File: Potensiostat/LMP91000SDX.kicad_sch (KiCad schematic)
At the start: 5 parts, among them J1 Conn_01x03_Pin, U2 LMP91000SDX/NOPB

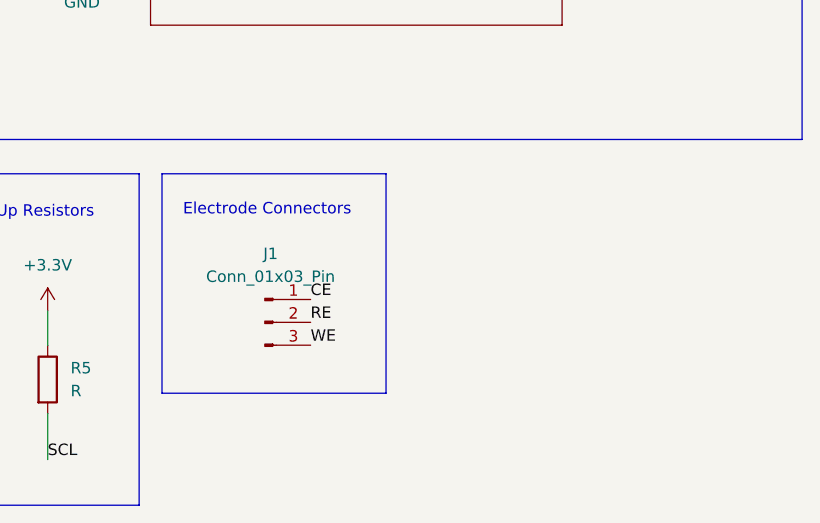
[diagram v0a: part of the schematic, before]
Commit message: Added LMP USP-UART
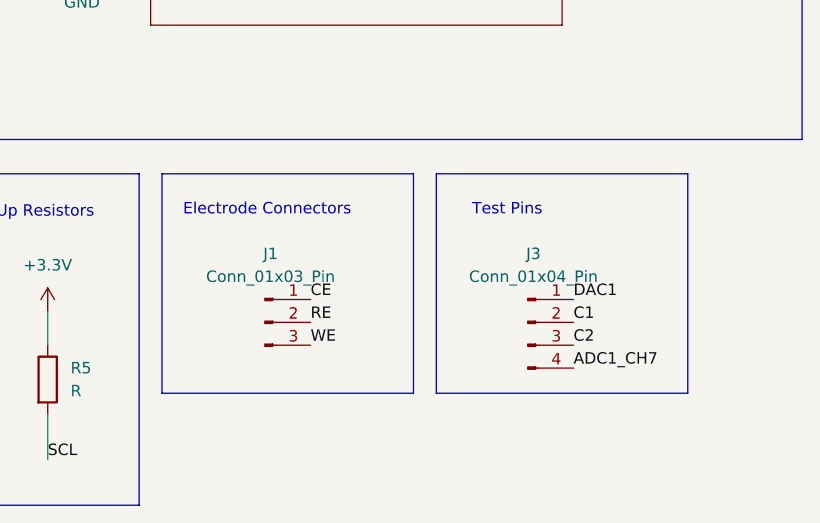
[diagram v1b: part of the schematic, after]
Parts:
- added J3: Conn_01x04_Pin, symbol Connector:Conn_01x04_Pin
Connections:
- net ADC1_CH7: now also J3.4 (Pin_4)
- net C1: now also J3.2 (Pin_2)
- net C2: now also J3.3 (Pin_3)
- net DAC1: now also J3.1 (Pin_1)
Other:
- note added: "Test Pins"
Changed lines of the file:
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@@
 	(rectangle
 		(start 53.34 107.95)
-		(end 78.232 132.334)
+		(end 81.28 132.334)
+		(stroke
+			(width 0)
+			(type default)
+		)
+		(fill
+			(type none)
+		)
+	)
+	(rectangle
+		(start 83.82 107.95)
+		(end 111.76 132.334)
 		(stroke
 			(width 0)
@@
 		(exclude_from_sim no)
 		(at 25.654 21.082 0)
+		(effects
+			(font
+				(size 1.27 1.27)
+			)
+		)
+	)
+	(text "Test Pins"
+		(exclude_from_sim no)
+		(at 91.694 112.014 0)
 		(effects
 			(font
@@
 		)
 	)
+	(label "C2"
+		(at 99.06 127 0)
+		(effects
+			(font
+				(size 1.27 1.27)
+			)
+			(justify left bottom)
+		)
+	)
 	(label "SDA"
 		(at 44.45 76.2 180)
@@
 		)
 	)
+	(label "C1"
+		(at 99.06 124.46 0)
+		(effects
+			(font
+				(size 1.27 1.27)
+			)
+			(justify left bottom)
+		)
+	)
 	(label "SCL"
 		(at 44.45 73.66 180)
@@
 		)
 	)
+	(label "DAC1"
+		(at 99.06 121.92 0)
+		(effects
+			(font
+				(size 1.27 1.27)
+			)
+			(justify left bottom)
+		)
+	)
 	(label "C1"
 		(at 105.41 81.28 0)
@@
 	(label "WE"
 		(at 105.41 76.2 0)
+		(effects
+			(font
+				(size 1.27 1.27)
+			)
+			(justify left bottom)
+		)
+	)
+	(label "ADC1_CH7"
+		(at 99.06 129.54 0)
 		(effects
 			(font
@@
 					(unit 1)
 				)
+			)
+		)
+	)
+	(symbol
+		(lib_id "Connector:Conn_01x04_Pin")
+		(at 93.98 124.46 0)
+		(unit 1)
+		(exclude_from_sim no)
+		(in_bom yes)
+		(on_board yes)
+		(dnp no)
+		(fields_autoplaced yes)
+		(property "Reference" "J3"
+			(at 94.615 116.84 0)
+			(effects
+				(font
+					(size 1.27 1.27)
+				)
+			)
+		)
+		(property "Value" "Conn_01x04_Pin"
+			(at 94.615 119.38 0)
+			(effects
+				(font
+					(size 1.27 1.27)
+				)
+			)
+		)
+		(property "Footprint" ""
+			(at 93.98 124.46 0)
+			(effects
+				(font
+					(size 1.27 1.27)
+				)
+				(hide yes)
+			)
+		)
+		(property "Datasheet" "~"
+			(at 93.98 124.46 0)
+			(effects
+				(font
+					(size 1.27 1.27)
+				)
+				(hide yes)
+			)
+		)
+		(property "Description" "Generic connector, single row, 01x04, script generated"
+			(at 93.98 124.46 0)
+			(effects
+				(font
+					(size 1.27 1.27)
+				)
+				(hide yes)
+			)
+		)
+		(pin "4"
+		)
+		(pin "1"
+		)
+		(pin "2"
+		)
+		(pin "3"
+		)
+		(instances
+			(project ""
+				(path "/be108998-ac86-4f7d-931a-841db1905f2a/62dba8b7-8e77-43af-b2ef-391554dc76c9"
+					(reference "J3")
+					(unit 1)
+				)
